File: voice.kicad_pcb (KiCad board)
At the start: 2 copper layers, 133.3 x 50 mm, 420 parts, among them J1 DDR3-DIMM, Q1 2SA1832, Q10 2SA1832, Q11 2SA1832, Q12 2SK208-GR, Q13 2SK208-GR, Q14 2SA1832, Q15 2SA1832, Q16 2SA1618, Q17 2SA1832, Q18 2SA1832, Q19 2SK208-GR, Q2 2SA1832, Q20 2SA1832, Q21 2SC4738, Q22 2SC4738, Q23 2SC4738, Q24 2SC4207, Q25 2SA1618, Q26 2SA1618, Q27 2SC4207, Q28 2SC4738, Q29 MMBF4391LT1G, Q3 2SA1832, Q30 MMBF4391LT1G, Q31 2SC4207, Q32 2SC4207, Q33 PMBT2369, Q34 PMBT2369, Q35 2SA1832, Q36 2SA1832, Q37 PMBT2369, Q38 2SC4738, Q4 2SA1832, Q5 2SK208-GR, Q6 2SK208-GR, Q7 2SK208-GR, Q8 2SK208-GR, Q9 2SK208-GR, U1 CD4053, U10 LM13700, U11 TL072-, U12 LM13700, U13 TA75S558F, U14 LM13700, U15 RC4558, U16 TA75S558F, U17 NE555, U18 NE555, U19 TL074-, U2 LM13700, U20 CD4052, U21 CD4052, U22 TL074-, U23 TL072-, U24 TL074-, U25 TA75S558F, U26 TL072-, U27 TL074-, U3 TA75S558F, U30 CD4052, U31 CD4052, U4 CD4053, U5 LM13700, U6 TA75S558F, U7 LM13700, U8 LM13700, U9 LM13700

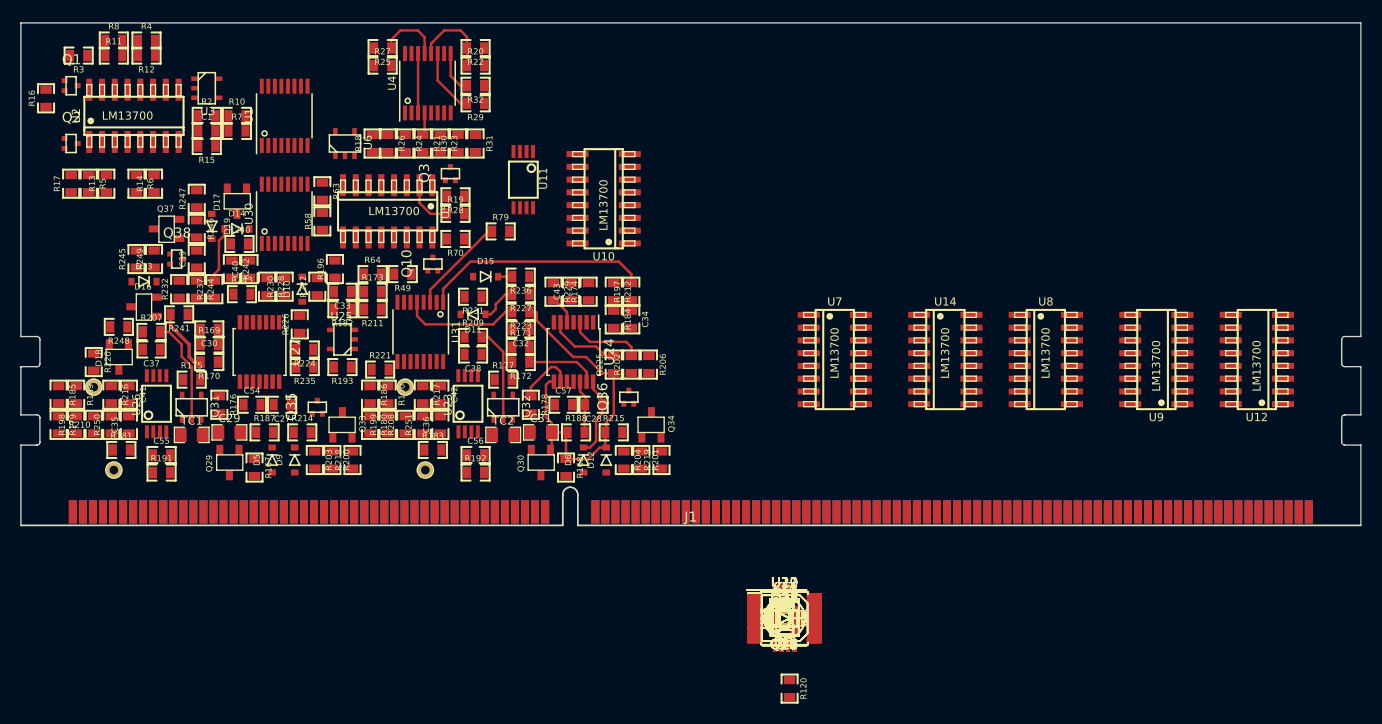
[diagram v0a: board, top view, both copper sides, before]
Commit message: startign to place VCF
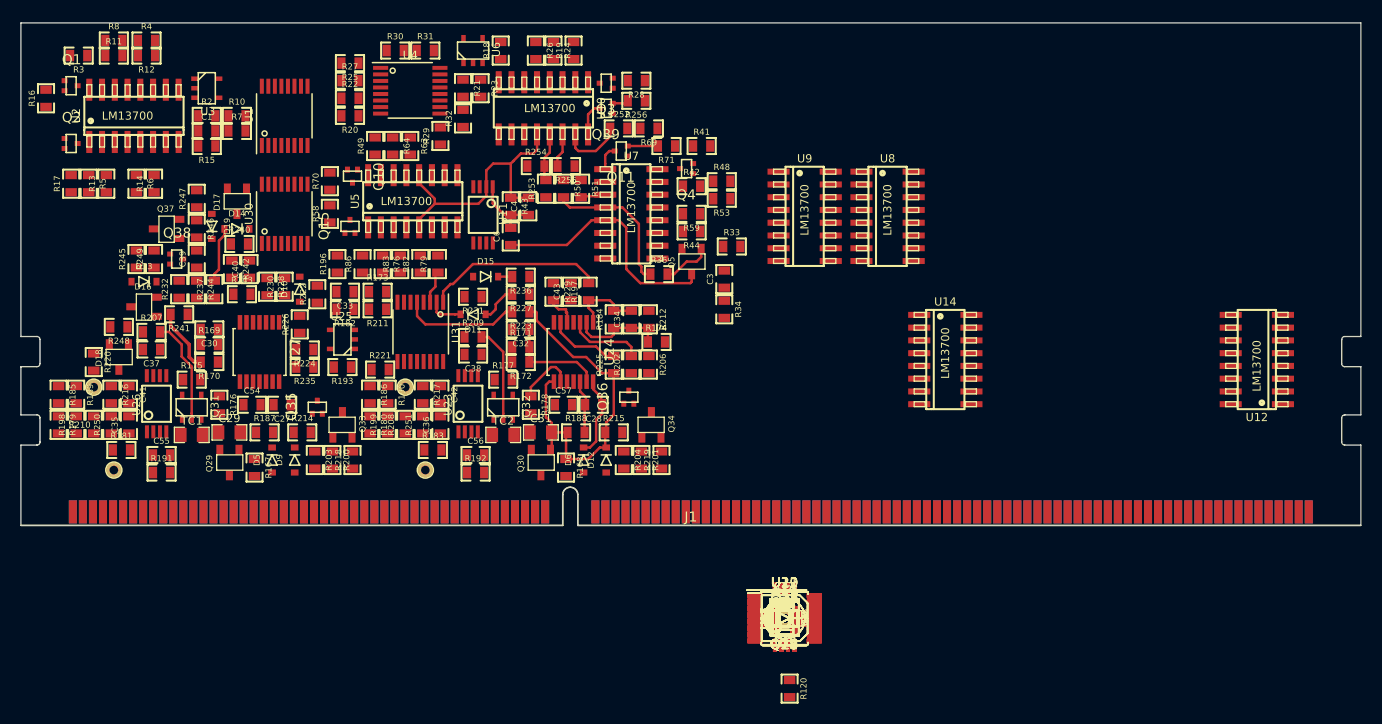
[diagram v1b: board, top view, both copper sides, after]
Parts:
- added Q39: 2SA1832, MyModules:SOT416-SC75, F.Cu at (143.2, 34.0)
- added R252: 12K, MyModules:SM0603-R-JRL, F.Cu at (144.5, 36.0)
- added R253: 47K, MyModules:SM0603-R-JRL, F.Cu at (137.2, 42.0)
- added R254: 470, MyModules:SM0603-R-JRL, F.Cu at (136.2, 39.8)
- added R255: 470, MyModules:SM0603-R-JRL, F.Cu at (139.2, 39.8)
- added R256: 18K, MyModules:SM0603-R-JRL, F.Cu at (146.2, 33.2)
- moved Q15 58.2 mm to (117.8, 45.8), turned to 270 degrees
- moved R86 54.8 mm to (119.0, 49.5), turned to 90 degrees
- moved R76 53.3 mm to (121.0, 49.5), turned to 270 degrees
- moved R83 52.0 mm to (122.8, 49.5), turned to 90 degrees
- moved R69 50.6 mm to (147.5, 36.0), turned to 180 degrees
- moved R82 50.6 mm to (124.8, 49.5), turned to 90 degrees
- moved Q11 49.3 mm to (144.8, 38.2)
- moved R43 49.2 mm to (133.8, 43.8), turned to 270 degrees
- moved R71 48.5 mm to (149.2, 37.8), turned to 180 degrees
- moved C4 48.3 mm to (135.5, 43.8), turned to 90 degrees
- moved R50 48.1 mm to (139.0, 42.0), turned to 270 degrees
- moved R41 47.7 mm to (152.8, 37.8)
- moved R51 47.3 mm to (140.8, 42.0), turned to 270 degrees
- moved C6 46.8 mm to (133.8, 46.8), turned to 90 degrees
- moved Q4 45.8 mm to (151.2, 40.0)
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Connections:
- J1 pad 107: Net-(J1-Pad107) -> AUX_LEVEL
- J1 pad 108: Net-(J1-Pad108) -> AUX
- U10 pad 1: Net-(U10-Pad1) -> Net-(Q3-Pad3)
- U10 pad 13: Net-(R79-Pad2) -> Net-(R253-Pad2)
- U10 pad 14: Net-(R83-Pad2) -> Net-(R255-Pad2)
- U10 pad 15: Net-(R76-Pad1) -> Net-(R252-Pad1)
- U10 pad 16: Net-(Q15-Pad3) -> Net-(Q39-Pad3)
- U10 pad 2: Net-(U10-Pad2) -> Net-(R19-Pad1)
- U10 pad 3: Net-(U10-Pad3) -> Net-(R21-Pad2)
- U10 pad 4: Net-(U10-Pad4) -> Net-(R24-Pad2)
- U10 pad 5: Net-(U10-Pad5) -> Net-(C2-Pad1)
- U4 pad 10: Net-(U4-Pad10) -> Net-(R32-Pad2)
- U4 pad 11: Net-(R29-Pad2) -> Net-(U4-Pad11)
- U4 pad 12: Net-(R20-Pad1) -> Net-(U4-Pad12)
- U4 pad 13: Net-(R25-Pad1) -> Net-(U4-Pad13)
- U4 pad 15: Net-(U4-Pad15) -> Net-(R21-Pad1)
- U4 pad 2: Net-(U4-Pad2) -> Net-(R30-Pad2)
- U4 pad 3: Net-(U4-Pad14) -> Net-(R25-Pad1)
- U4 pad 4: Net-(R21-Pad1) -> Net-(U4-Pad1)
- U4 pad 5: Net-(R30-Pad2) -> Net-(R20-Pad1)
- U4 pad 9: Net-(R32-Pad2) -> Net-(R29-Pad2)
- U5 pad 1: Net-(Q3-Pad3) -> Net-(Q15-Pad3)
- U5 pad 2: Net-(R19-Pad1) -> Net-(R76-Pad1)
- U5 pad 3: Net-(R21-Pad2) -> Net-(R83-Pad2)
- U5 pad 4: Net-(R24-Pad2) -> Net-(R79-Pad2)
- U5 pad 5: Net-(C2-Pad1) -> Net-(C4-Pad2)
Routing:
- net Net-(C4-Pad2): track 0.00 -> 27.0 mm
- net Net-(C6-Pad1): track 0.00 -> 25.6 mm
- net Net-(R36-Pad1): track 0.00 -> 14.7 mm
- net Net-(C34-Pad1): track 0.00 -> 9.57 mm
- net Net-(R20-Pad1): track 8.23 -> 0.00 mm
- net Net-(C34-Pad2): track 0.00 -> 7.45 mm
- net Net-(C4-Pad1): track 0.00 -> 6.97 mm
- net Net-(R29-Pad2): track 6.55 -> 0.00 mm
- net VCO2: track 9.82 -> 3.37 mm
- net Net-(R25-Pad1): track 6.43 -> 0.00 mm
- net Net-(R252-Pad1): track 0.00 -> 6.36 mm
- net Net-(U4-Pad14): track 5.90 -> 0.00 mm
- net Net-(R19-Pad1): track 4.94 -> 0.00 mm
- net Net-(C3-Pad2): track 0.00 -> 4.87 mm
- net Net-(R253-Pad2): track 0.00 -> 4.83 mm
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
